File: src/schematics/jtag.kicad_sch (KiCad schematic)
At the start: 0 parts

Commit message: ✅ Validate the schematic symbols (#33)
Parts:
- added U6: ~, symbol ECAP5-BSOM:LFE5U-85F-*BG756*

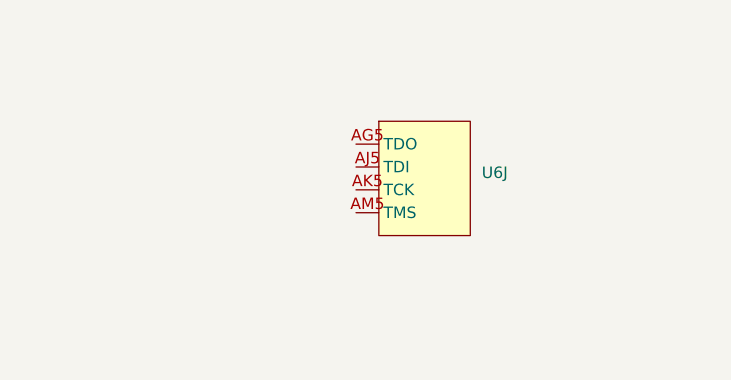
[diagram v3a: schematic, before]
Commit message: ✨ Add FPGA jtag circuit
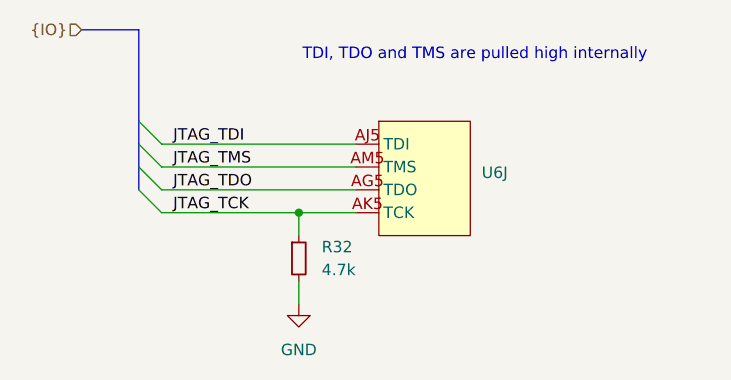
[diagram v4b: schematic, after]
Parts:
- added R32: 4.7k, symbol Device:R_Small
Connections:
- net JTAG_TDO: now reaches U6.AG5 (TDO)
- net JTAG_TDI: now reaches U6.AJ5 (TDI)
- net JTAG_TCK: now reaches U6.AK5 (TCK)
- net JTAG_TCK: now also R32.1
- net JTAG_TMS: now reaches U6.AM5 (TMS)
- new net GND: R32.2
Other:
- note added: "TDI, TDO and TMS are pulled high internally"

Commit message: Add footprint for ecp5 (#75)
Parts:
- U6: footprint (none) -> ECAP5-DPROC:LFE5U-85F-_BG756C
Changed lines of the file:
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@@
 			)
 		)
-		(property "Footprint" ""
+		(property "Footprint" "ECAP5-DPROC:LFE5U-85F-_BG756C"
 			(at 158.75 82.55 0)
 			(effects

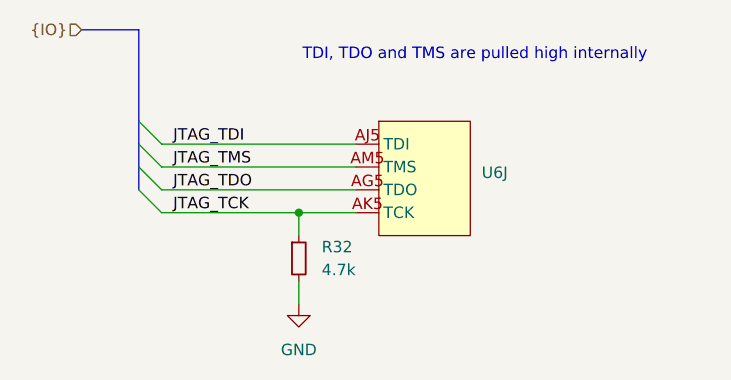
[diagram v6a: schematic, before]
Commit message: Add footprint for the io connector
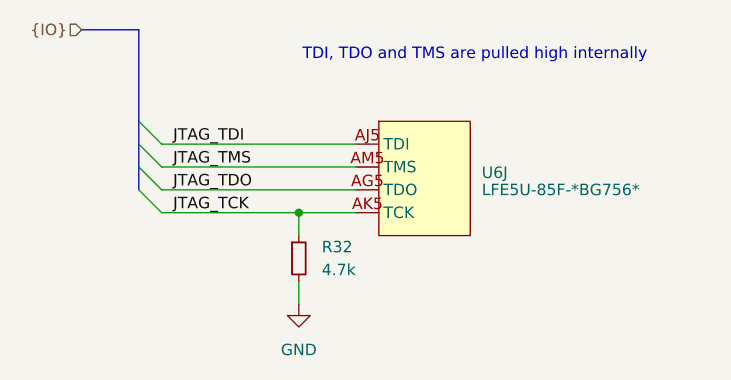
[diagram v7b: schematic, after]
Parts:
- U6: value ~ -> LFE5U-85F-*BG756*
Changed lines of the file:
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@@
 			)
 		)
-		(property "Value" "~"
+		(property "Value" "LFE5U-85F-*BG756*"
 			(at 166.37 87.63 0)
 			(effects

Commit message: Add remaining component footprints (#79)
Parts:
- R32: footprint (none) -> Resistor_SMD:R_0603_1608Metric
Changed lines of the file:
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@@
 			)
 		)
-		(property "Footprint" ""
+		(property "Footprint" "Resistor_SMD:R_0603_1608Metric"
 			(at 146.05 95.25 0)
 			(effects
